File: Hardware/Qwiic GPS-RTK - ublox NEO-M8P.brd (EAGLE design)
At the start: 40.6 x 33 mm, 103 parts, among them J13 U.FL, J3 PTH, U1 NEO-M8P, U2 3.3V

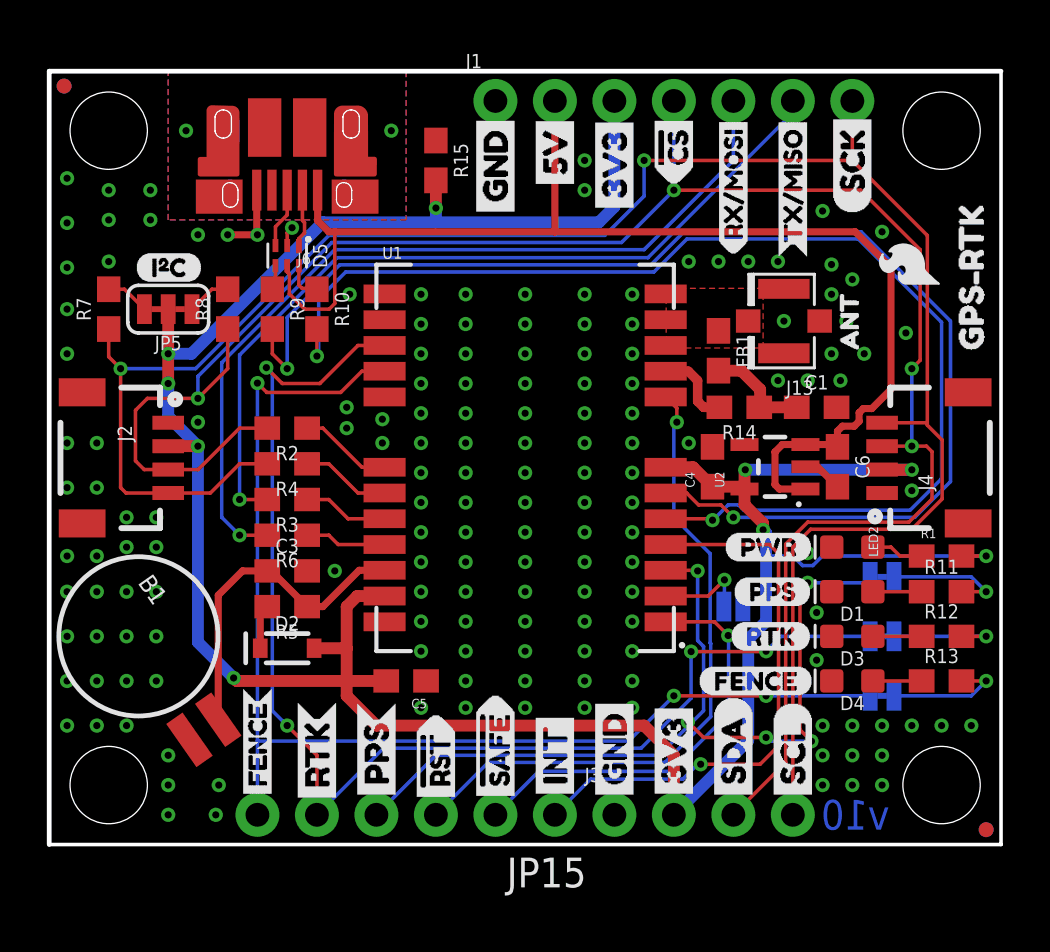
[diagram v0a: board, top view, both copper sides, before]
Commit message: Adds reflowable battery and moves all parts to use SparkFun Libraries
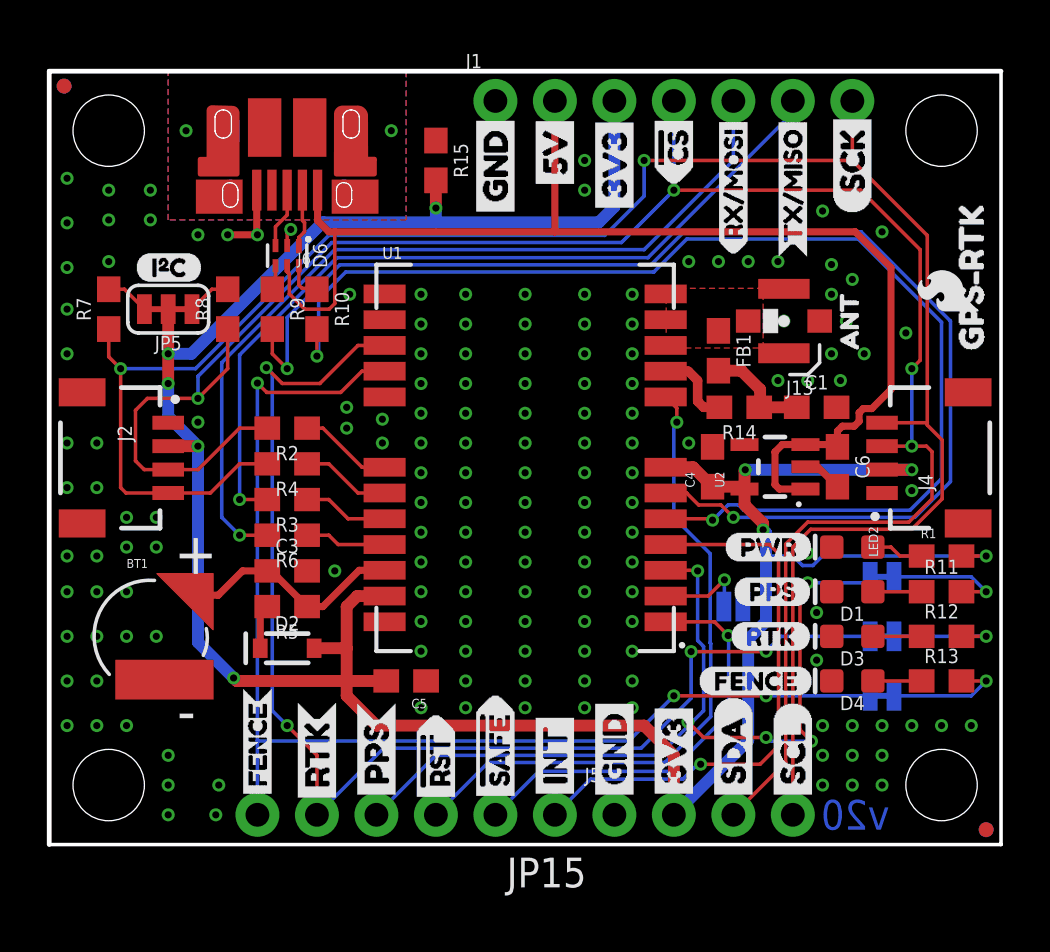
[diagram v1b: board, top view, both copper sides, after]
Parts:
- removed B1: 6.8MM_COIN_CELL, SparkFun-Batteries:BATTCON-6.8MM
- removed D5: PRTR5V0U2F, funbit:SOT886
- removed J3: PTH, SparkX:1X04_NO_SILK
- added BT1: ML414H_IV01E_BATTERY, SparkFun-Batteries:ML414H_IV01E
- added D6: PRTR5V0U2F, SparkFun-IC-Power:SOT886
- added J5: (no value), SparkFun-Connectors:1X04_NO_SILK
- J2, J4: value (none) -> Qwiic Right Angle; device SparkFun-Connectors:1X04_1MM_RA -> SparkFun-Connectors:JST04_1MM_RA
- JP1, JP2, JP3: value (none) -> JUMPER-SMT_2_NC_TRACE_SILK
- JP101, JP31, JP41, JP91: value STAND-OFF -> STAND-OFFTIGHT; device SparkFun:STAND-OFF -> SparkFun-Hardware:STAND-OFF-TIGHT
- JP21, JP61, JP71, JP81: device SparkFun:MICRO-FIDUCIAL -> SparkFun-Aesthetics:FIDUCIAL-MICRO
- JP4: value (none) -> JUMPER-SMT_2_NO_SILK
- JP5: value (none) -> JUMPER-SMT_3_2-NC_TRACE_SILK
- U1: device NEO-M8P:NEO-M8P -> SparkFun-GPS:NEO-M8P
- moved FRAME1 9.91 mm to (-7.87, -17.8)
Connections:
- net 3.3V: now also J5.2; no longer J3.2
- net 5V: now also D6.5; no longer D5.5
- net BACKUP: now also BT1.+; no longer B1.+
- net D+: now also D6.4; no longer D5.4
- net D-: now also D6.6; no longer D5.6
- net GND: now also BT1.-, D6.2, J5.1; no longer B1.-, D5.2, J3.1
- net SCL/SCK: now also J5.4; no longer J3.4
- net SDA/!CS: now also J5.3; no longer J3.3
- net USB_D+: now also D6.3; no longer D5.3
- net USB_D-: now also D6.1; no longer D5.1
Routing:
- net BACKUP: track 14.1 -> 9.80 mm
- net GND: track 5.71 -> 5.61 mm, vias 161 -> 158
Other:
- board text added: "+"
- board text added: "-"
- board text added: "Nathan Seidle"
- board text added: "Revised By: Elias Santistevan"
- board text added: "v20"
- board text removed: "v10"
